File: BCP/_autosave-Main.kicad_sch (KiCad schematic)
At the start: 7 parts, among them SW1 SW_Nidec_CAS-120A1, U1 LD1117V33, U2 Pico 2, U3 DEV-13712

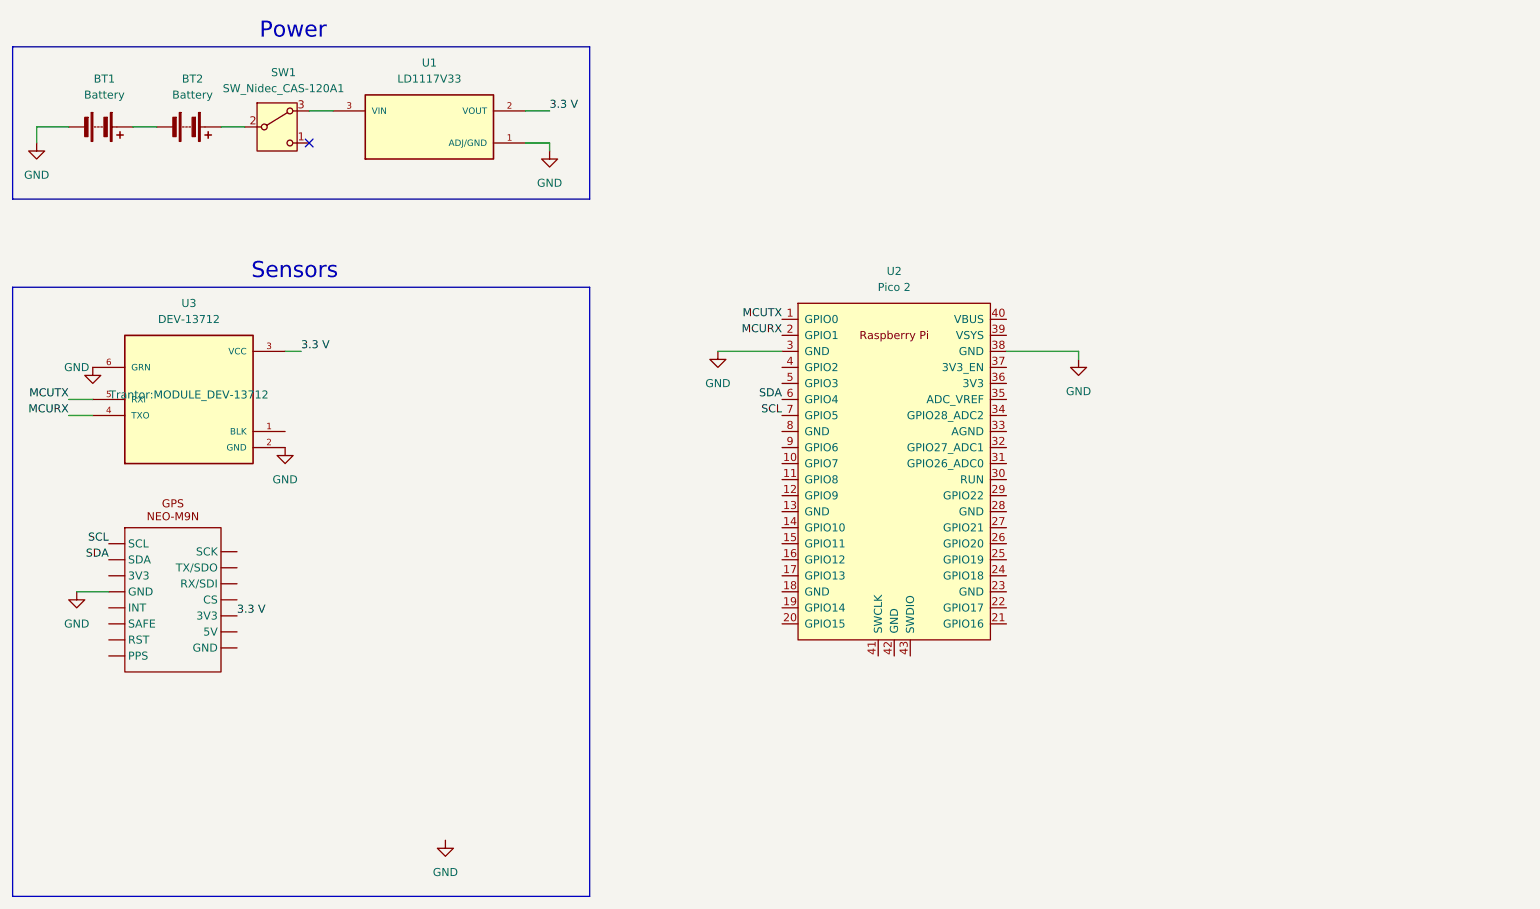
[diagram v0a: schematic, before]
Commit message: Added GPS (somewhat)
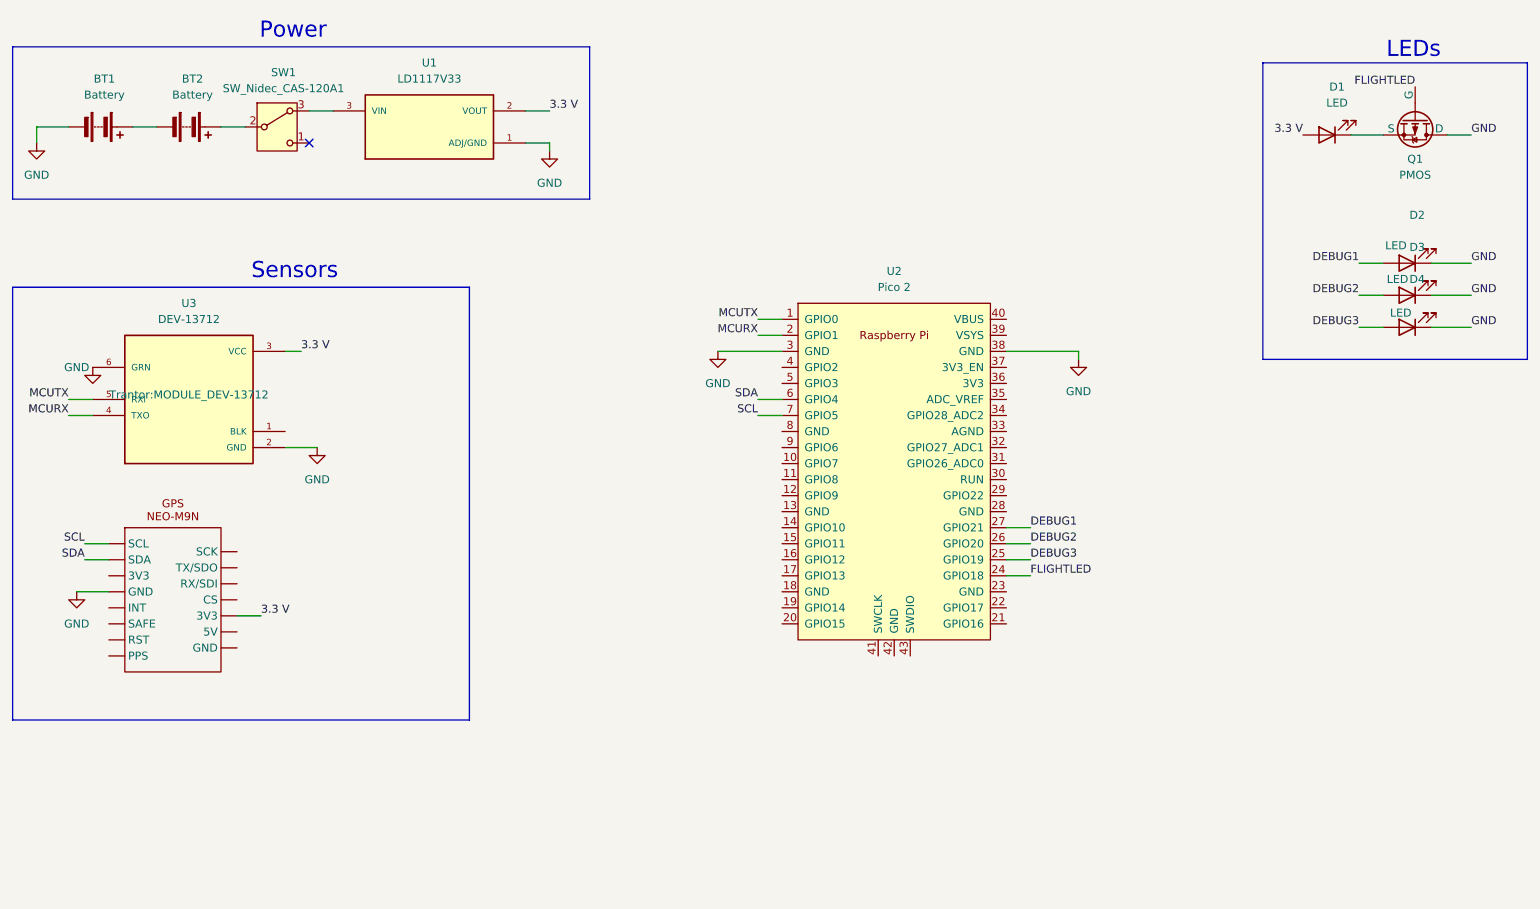
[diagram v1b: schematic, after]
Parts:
- added D1, D2, D3, D4: LED, symbol Device:LED
- added Q1: PMOS, symbol Simulation_SPICE:PMOS
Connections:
- net 3.3 V: now also D1.2 (A)
- net GND: now also D2.1 (K), D3.1 (K), D4.1 (K), Q1.1 (D)
- net FLIGHTLED: now reaches U2.24 (GPIO18)
- net FLIGHTLED: now also Q1.2 (G)
- net DEBUG3: now reaches U2.25 (GPIO19)
- net DEBUG3: now also D4.2 (A)
- net DEBUG2: now reaches U2.26 (GPIO20)
- net DEBUG2: now also D3.2 (A)
- net DEBUG1: now reaches U2.27 (GPIO21)
- net DEBUG1: now also D2.2 (A)
- new net: D1.1 (K), Q1.3 (S)
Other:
- note added: "LEDs"
